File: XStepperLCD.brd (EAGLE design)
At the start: 72.1 x 31.7 mm, 31 parts, among them Q2 16 MHZ, U1 LCD-16X2NOHOLES

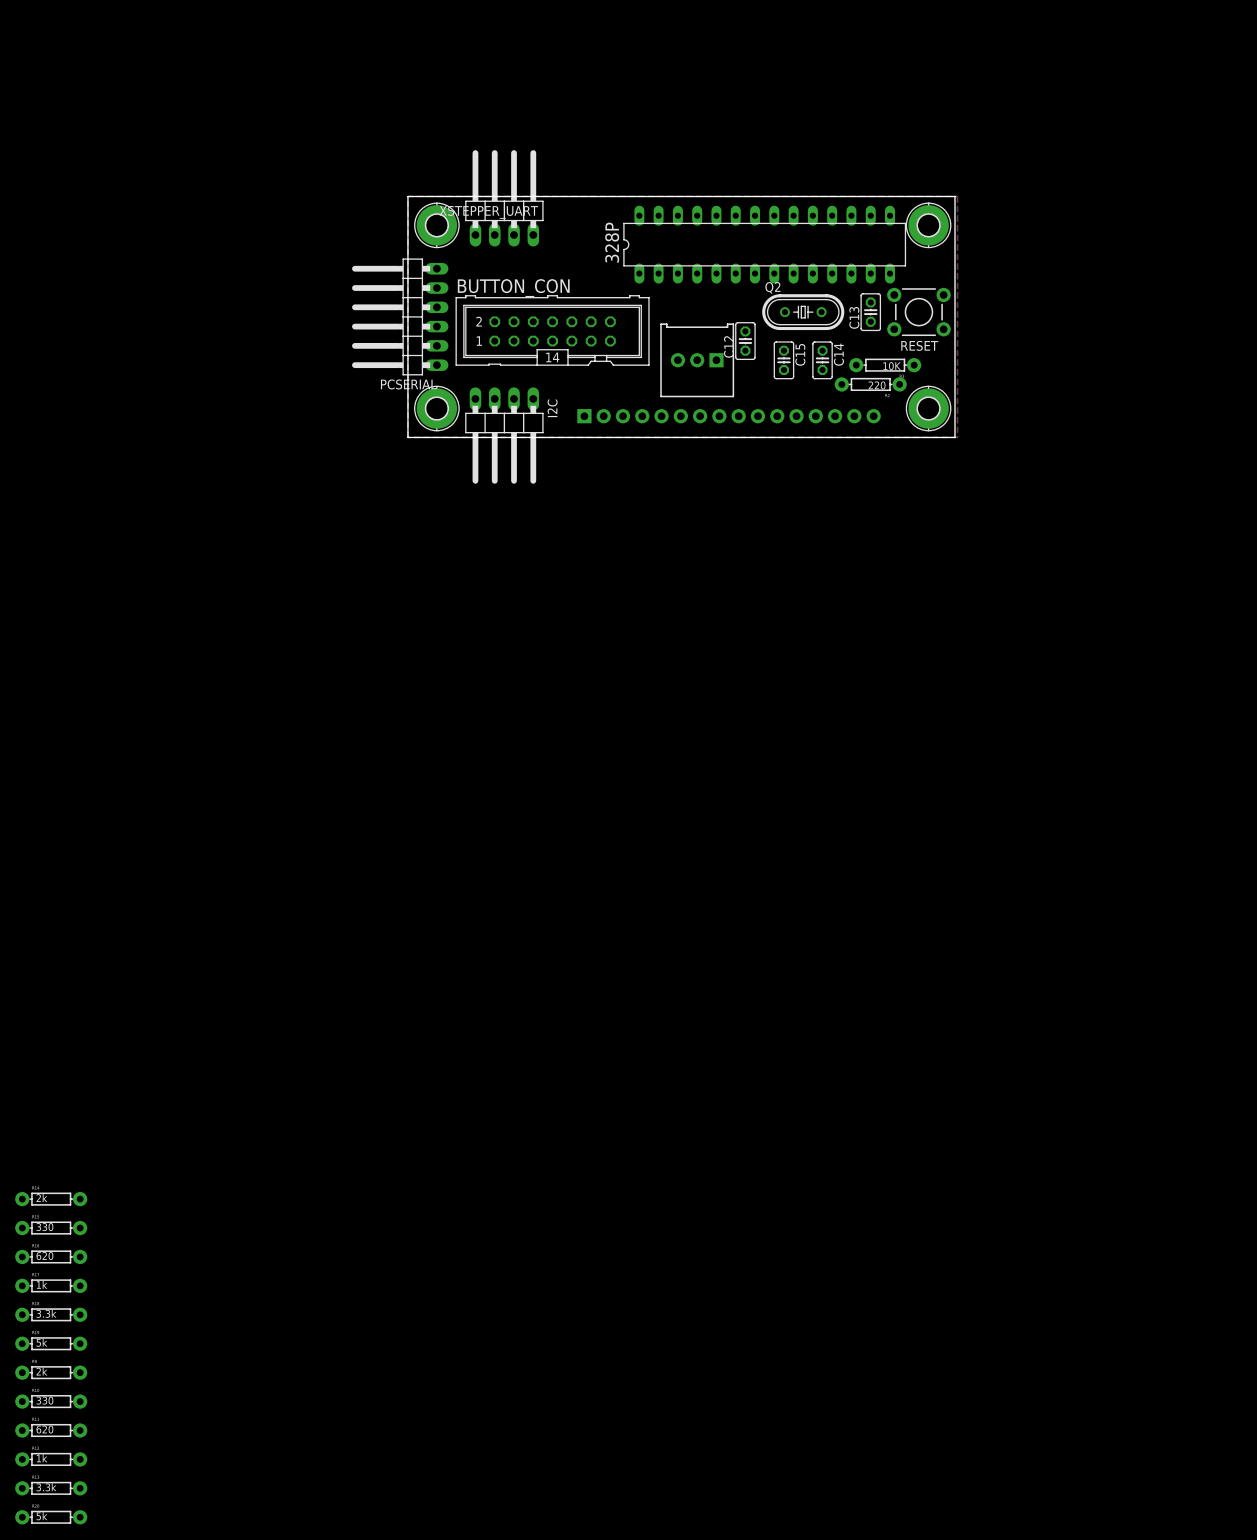
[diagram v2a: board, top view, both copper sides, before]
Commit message: pov, duo led, sketchup
- add duo led
- add icsp header
- create povray file
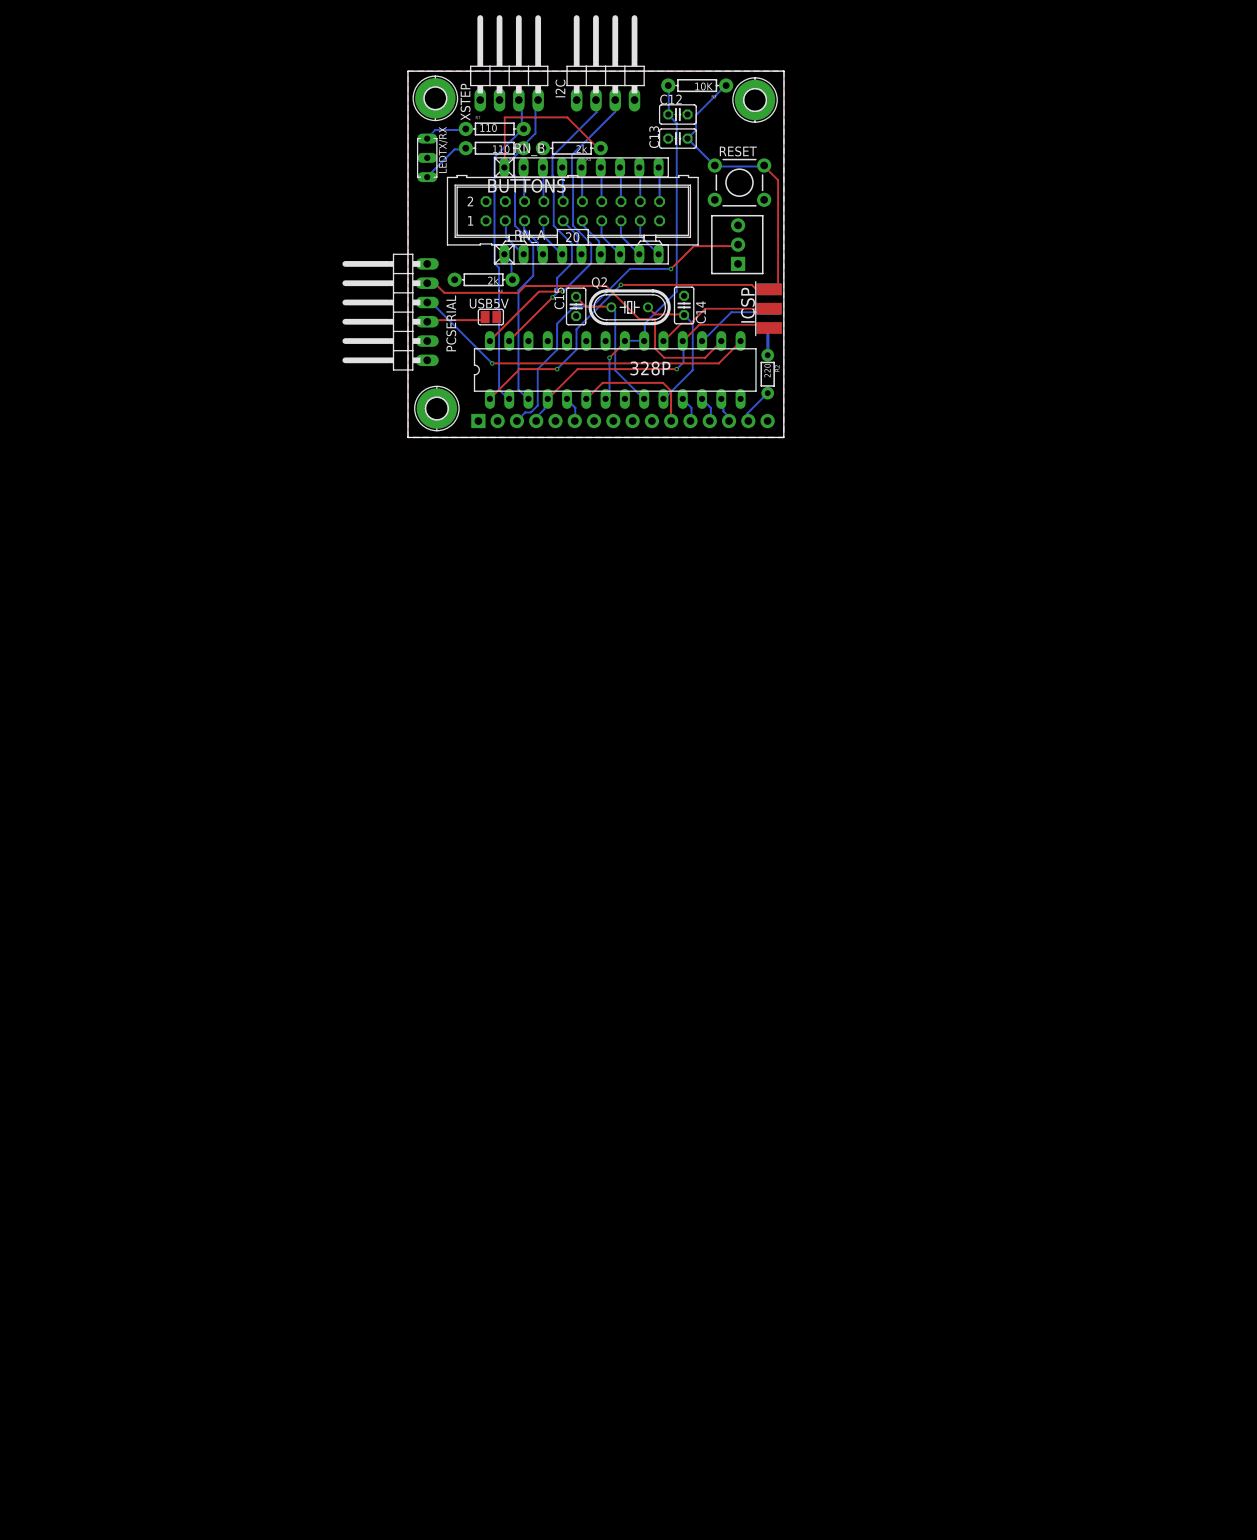
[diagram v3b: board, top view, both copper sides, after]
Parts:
- removed BUTTON_CON: (no value), con-ml:ML14
- removed H8: MOUNT-PAD-ROUND2.8, holes:2,8-PAD
- removed R10, R15: 330, SparkFun-Resistors:AXIAL-0.3
- removed R11, R16: 620, SparkFun-Resistors:AXIAL-0.3
- removed R12, R17: 1k, SparkFun-Resistors:AXIAL-0.3
- removed R13, R18: 3.3k, SparkFun-Resistors:AXIAL-0.3
- removed R14, R9: 2k, SparkFun-Resistors:AXIAL-0.3
- removed R19, R20: 5k, SparkFun-Resistors:AXIAL-0.3
- removed XSTEPPER_UART: serial, pinhead:1X04/90
- added BUTTONS: (no value), con-ml:ML20
- added ICSP: ICSP, avr-7:6PAD_ISP
- added LEDTX/RX: (no value), led:DUOLED2X5
- added R4, R5: 2k, SparkFun-Resistors:AXIAL-0.3
- added R6, R7: 110, SparkFun-Resistors:AXIAL-0.3
- added RN_A, RN_B: 330, resistor-net:RN-9
- added USB5V: (no value), jumper:SJ
- added XSTEP: serial, pinhead:1X04/90
- R1: device SparkFun-Electromechanical:3386U -> SparkFun-Electromechanical:3362U-2
- R2: device SparkFun-Resistors:AXIAL-0.3 -> SparkFun-Resistors:1/6W-RES
- moved I2C 48.8 mm to (26.0, 48.3), turned to 0 degrees
- moved R3 44.4 mm to (38.1, 46.4)
- moved C13 34.2 mm to (35.6, 39.4), turned to 0 degrees
- moved C12 31.1 mm to (35.6, 42.5), turned to 180 degrees
- moved RESET 29.2 mm to (43.7, 33.6)
- moved C15 28.3 mm to (22.2, 17.3)
- moved H6 28.2 mm to (45.7, 44.5)
- moved 328P 25.7 mm to (27.3, 8.89)
- moved Q2 22.9 mm to (29.2, 17.1)
- moved C14 19.6 mm to (36.4, 17.4), turned to 90 degrees
- moved H5 16.7 mm to (3.61, 44.7)
- moved R1 16.1 mm to (43.2, 25.4), turned to 90 degrees
- moved U1 14.0 mm to (41.3, -13.3)
- moved R2 13.6 mm to (47.4, 8.34), turned to 270 degrees
- moved PCSERIAL 1.42 mm to (-1.27, 16.5)
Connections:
- removed net RS: 328P.4, U1.4
- new net MOSI: 328P.17, ICSP.MOSI
- new net N$10: BUTTONS.5, RN_A.3
- new net N$17: BUTTONS.9, RN_A.5
- new net N$18: BUTTONS.11, RN_A.6
- new net N$19: BUTTONS.18, RN_B.8
- new net N$20: BUTTONS.20, RN_B.9
- new net N$21: LEDTX/RX.AG, R6.P$2
- new net N$22: LEDTX/RX.AR, R7.P$1
- new net N$7: BUTTONS.6, RN_B.2
- new net N$8: BUTTONS.8, RN_B.3
- new net N$9: BUTTONS.3, RN_A.2
- new net RS/MISO: 328P.18, 328P.4, ICSP.MISO, U1.4
- new net SCK: 328P.19, ICSP.SCK
- net BUTTONS_A: no longer BUTTON_CON.13, R10.P$1, R11.P$1, R12.P$1, R13.P$1, R20.P$1, R9.P$1
- net BUTTONS_B: no longer BUTTON_CON.14, R14.P$1, R15.P$2, R16.P$2, R17.P$2, R18.P$2, R19.P$2
- net D4: now also 328P.6
- net GND: now also BUTTONS.1, BUTTONS.19, BUTTONS.2, BUTTONS.4, ICSP.GND, LEDTX/RX.K, XSTEP.2; no longer BUTTON_CON.1, BUTTON_CON.2, H8.B2,8, XSTEPPER_UART.2
- net N$11: now also BUTTONS.10, RN_B.4; no longer BUTTON_CON.12, R15.P$1
- net N$12: now also BUTTONS.12, RN_B.5; no longer BUTTON_CON.10, R16.P$1
- net N$13: now also BUTTONS.14, RN_B.6; no longer BUTTON_CON.8, R17.P$1
- net N$14: now also R5.P$1, RN_B.1; no longer BUTTON_CON.6, R18.P$1
- net N$15: now also BUTTONS.16, RN_B.7; no longer BUTTON_CON.4, R19.P$1
- net N$16: now also BUTTONS.7, RN_A.4; no longer BUTTON_CON.3, R20.P$2
- net N$2: now also R2.2; no longer R2.P$2
- net N$3: now also R4.P$1, RN_A.1; no longer BUTTON_CON.11, R10.P$2
- net N$4: now also BUTTONS.13, RN_A.7; no longer BUTTON_CON.9, R11.P$2
- net N$5: now also BUTTONS.15, RN_A.8; no longer BUTTON_CON.7, R12.P$2
- net N$6: now also BUTTONS.17, RN_A.9; no longer BUTTON_CON.5, R13.P$2
- net RESET: now also ICSP.RST
- net RX: now also R6.P$1, XSTEP.4; no longer XSTEPPER_UART.4
- net TX: now also R7.P$2, XSTEP.3; no longer XSTEPPER_UART.3
- net USB_5V: now also USB5V.1
- net VCC: now also ICSP.VCC, R2.1, R4.P$2, R5.P$2, USB5V.2, XSTEP.1; no longer R14.P$2, R2.P$1, R9.P$2, XSTEPPER_UART.1
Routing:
- net RESET: track 0.00 -> 83.9 mm, vias 0 -> 2
- net 5V: track 0.00 -> 47.3 mm, vias 0 -> 1
- net USB_RXD: track 0.00 -> 46.8 mm
- net USB_TXD: track 0.00 -> 45.9 mm, vias 0 -> 1
- net N$1: track 0.00 -> 43.7 mm, vias 0 -> 1
- net RX: track 0.00 -> 43.2 mm
- net SCL: track 0.00 -> 42.5 mm, vias 0 -> 1
- net TX: track 0.00 -> 42.3 mm
- net RS/MISO: track 0.00 -> 38.7 mm, vias 0 -> 1
- net SDA: track 0.00 -> 38.7 mm, vias 0 -> 1
- net N$14: track 0.00 -> 20.9 mm
- net N$33: track 0.00 -> 19.1 mm
- net N$34: track 0.00 -> 18.3 mm
- net D4: track 0.00 -> 16.5 mm
- net SCK: track 0.00 -> 15.7 mm
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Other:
- board size 72.1 x 31.7 mm -> 49.5 x 48.3 mm
- board text added: "ICSP"

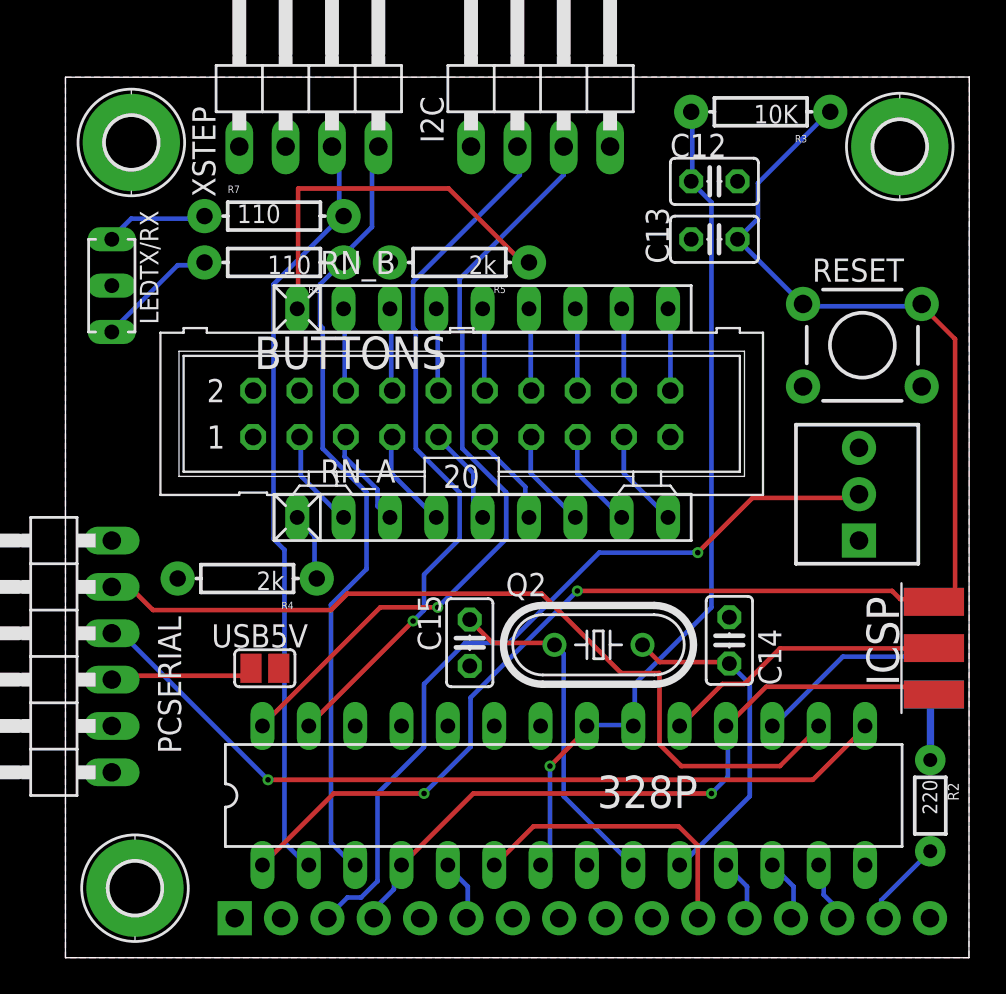
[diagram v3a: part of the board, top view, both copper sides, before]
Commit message: - add 2 connects for potentiometers
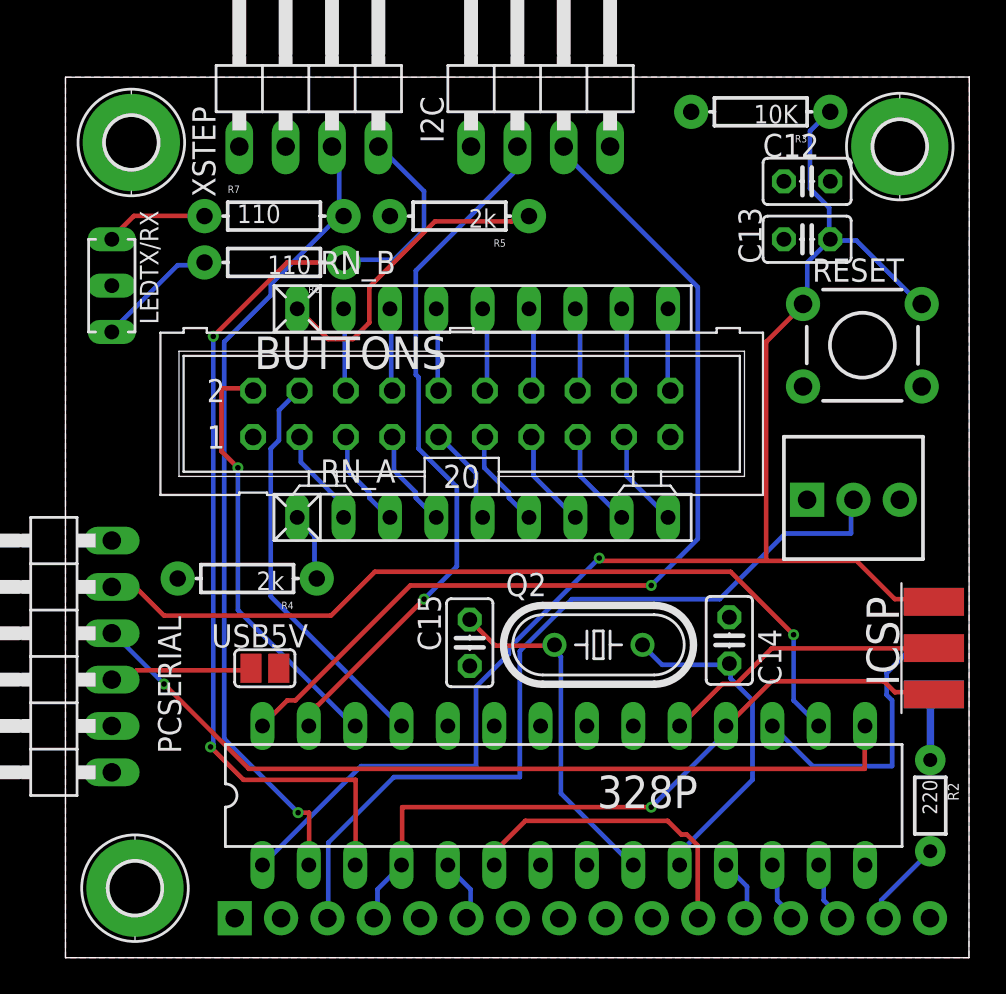
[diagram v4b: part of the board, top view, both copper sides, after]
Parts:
- moved C12 5.08 mm to (40.6, 42.5)
- moved C13 5.08 mm to (40.6, 39.4)
- moved R5 2.54 mm to (21.6, 40.6)
- turned R1 to 0 degrees
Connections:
- removed net 5V: 328P.20, 328P.21, 328P.7, C12.2, R3.P$2
- new net POT_A: 328P.25, BUTTONS.4
- new net POT_B: 328P.26, BUTTONS.2
- net GND: no longer BUTTONS.2, BUTTONS.4
- net VCC: now also 328P.20, 328P.21, 328P.7, C12.2, R3.P$2
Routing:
- net 5V: track 47.3 -> 0.00 mm, vias 1 -> 0
- net POT_B: track 0.00 -> 23.4 mm, vias 0 -> 1
- net POT_A: track 0.00 -> 22.0 mm
- net RX: track 43.2 -> 55.6 mm, vias 0 -> 2
- net SCL: track 42.5 -> 52.7 mm
- net MOSI: track 10.9 -> 15.8 mm
- net N$14: track 20.9 -> 17.4 mm
- net RESET: track 83.9 -> 81.0 mm, vias 2 -> 1
- net TX: track 42.3 -> 45.1 mm, vias 0 -> 1
- net N$1: track 43.7 -> 45.8 mm, vias 1 -> 0
- net USB_TXD: track 45.9 -> 46.8 mm
- net D4: track 16.5 -> 17.3 mm
- net USB_RXD: track 46.8 -> 46.0 mm, vias 0 -> 1
- net RS/MISO: track 38.7 -> 39.3 mm
